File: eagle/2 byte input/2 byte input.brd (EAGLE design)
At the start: 85.1 x 44.1 mm, 26 parts, among them IC1 74LS165N, IC2 74LS165N, X1 MKDSN1,5/5-5,08, X2 MKDSN1,5/5-5,08, X3 MKDSN1,5/8-5,08, X5 MKDSN1,5/8-5,08

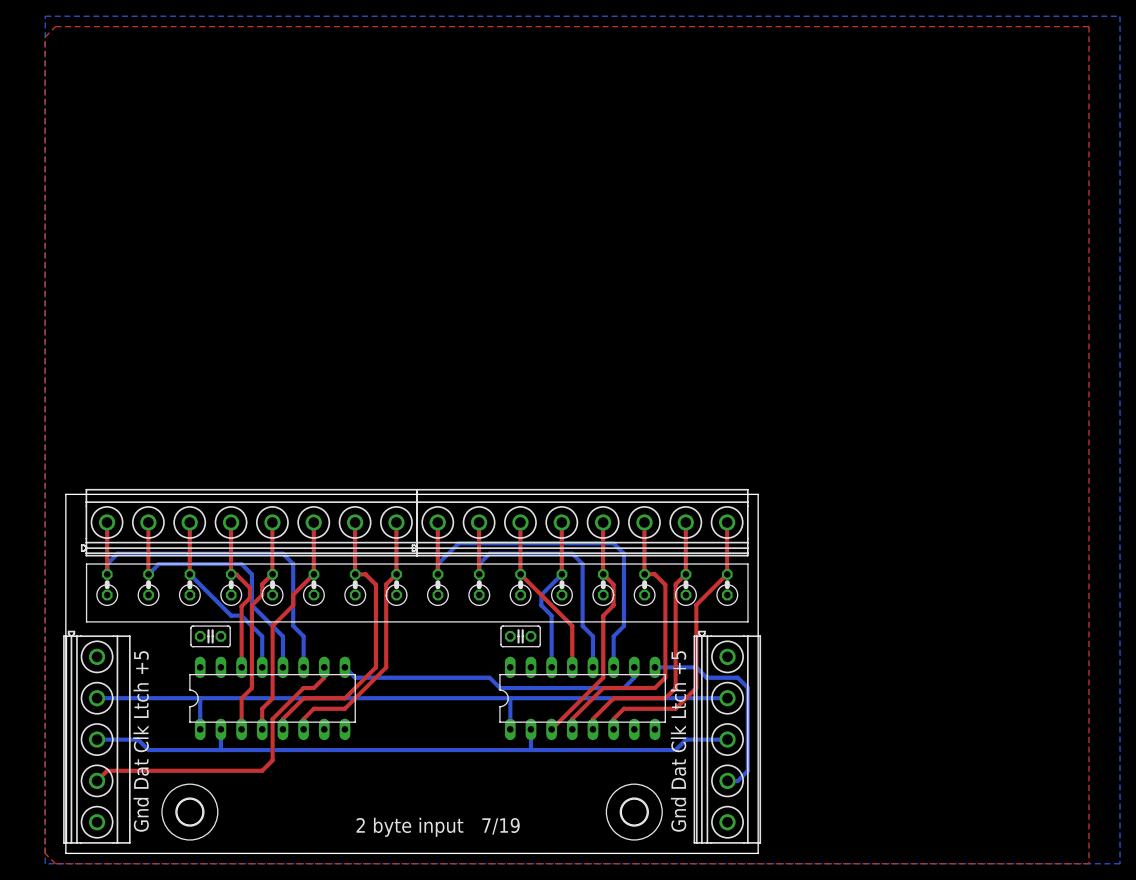
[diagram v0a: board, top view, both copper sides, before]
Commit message: corrected circuit for input board
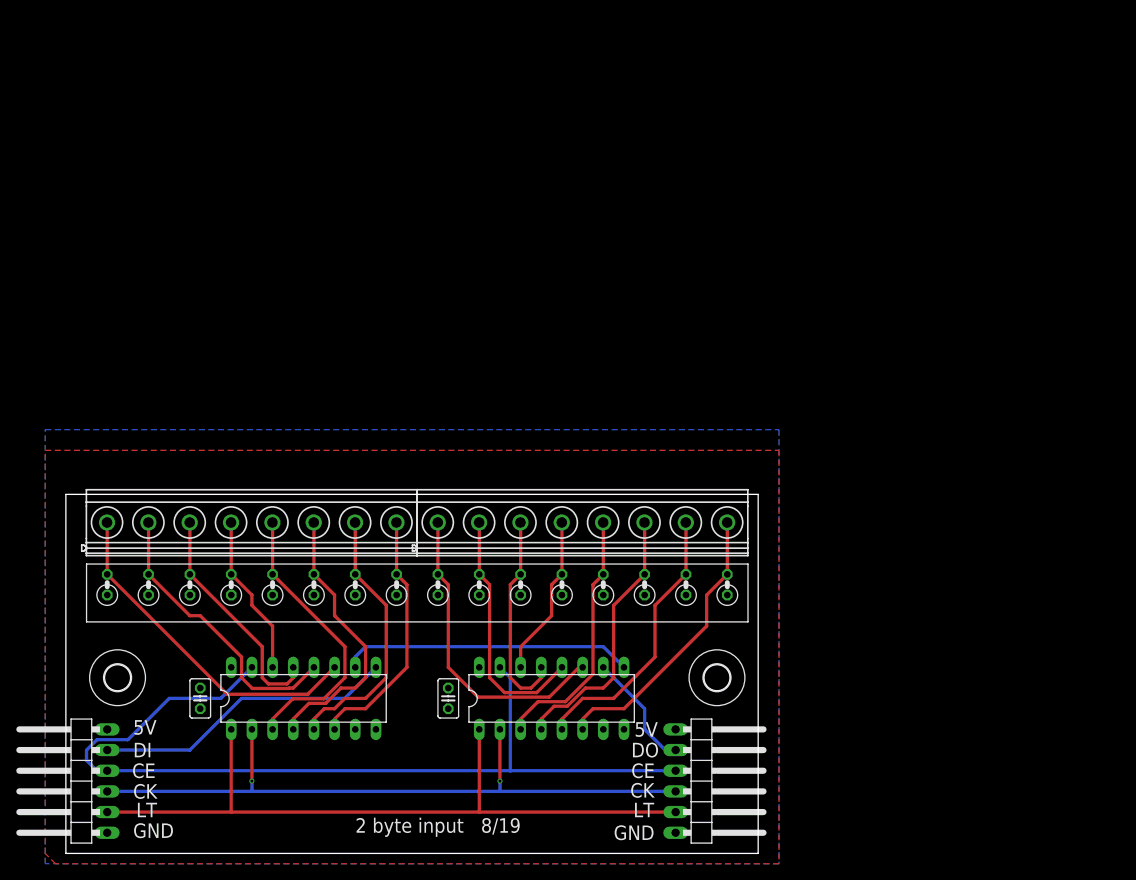
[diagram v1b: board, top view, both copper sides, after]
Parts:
- removed X1, X2: MKDSN1,5/5-5,08, con-phoenix-508:MKDSN1,5/5-5,08
- added JP1, JP2: (no value), pinhead:1X06/90
- moved H2 19.4 mm to (80.0, 21.6)
- moved H1 18.8 mm to (6.35, 21.6)
- moved C2 11.7 mm to (47.0, 19.1), turned to 270 degrees
- moved C1 7.73 mm to (16.5, 19.1), turned to 270 degrees
- moved IC1 3.81 mm to (29.2, 19.1)
- moved IC2 3.81 mm to (59.7, 19.1)
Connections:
- removed net SER0: IC1.10, X1.4
- removed net SER1: IC1.9, IC2.10
- removed net SERX: IC2.9, X2.4
- new net CE: IC1.15, IC2.15, JP1.4, JP2.3
- new net S0: IC1.9, JP1.5
- new net S1: IC1.10, IC2.9
- new net SX: IC2.10, JP2.2
- net +5V: now also JP1.6, JP2.1; no longer X1.1, X2.1
- net CLK: now also JP1.3, JP2.4; no longer X1.3, X2.3
- net GND: now also JP1.1, JP2.6; no longer IC1.15, IC2.15, X1.5, X2.5
- net LATCH: now also JP1.2, JP2.5; no longer X1.2, X2.2
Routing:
- net CE: track 0.00 -> 111.9 mm
- net SER1: track 38.4 -> 0.00 mm
- net SER0: track 37.4 -> 0.00 mm
- net S0: track 0.00 -> 37.2 mm
- net S1: track 0.00 -> 35.9 mm
- net SERX: track 25.7 -> 0.00 mm
- net SX: track 0.00 -> 14.6 mm
- net INB0: track 46.6 -> 37.9 mm
- net INA4: track 27.0 -> 35.0 mm
- net INA2: track 22.2 -> 28.5 mm
- net INA5: track 28.1 -> 34.0 mm
- net INB2: track 20.4 -> 25.7 mm
- net LATCH: track 85.1 -> 90.2 mm
- net INB1: track 34.6 -> 30.5 mm
- net INA0: track 44.8 -> 41.8 mm
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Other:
- board text added: "2 byte input 8/19"
- board text added: "5V"
- board text added: "CE"
- board text added: "CK"
- board text added: "DI"
- board text added: "DO"
- board text added: "GND"
- board text added: "LT"
- board text removed: "2 byte input 7/19"
- board text removed: "Gnd Dat Clk Ltch +5"
